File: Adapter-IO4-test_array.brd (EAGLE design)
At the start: 107.6 x 107.6 mm, 72 parts, among them Q1X11 p-fet, Q1X12 p-fet, Q1X21 p-fet, Q1X22 p-fet, Q2X11 p-fet, Q2X12 p-fet, Q2X21 p-fet, Q2X22 p-fet, Q3X11 p-fet, Q3X12 p-fet, Q3X21 p-fet, Q3X22 p-fet, Q4X11 p-fet, Q4X12 p-fet, Q4X21 p-fet, Q4X22 p-fet

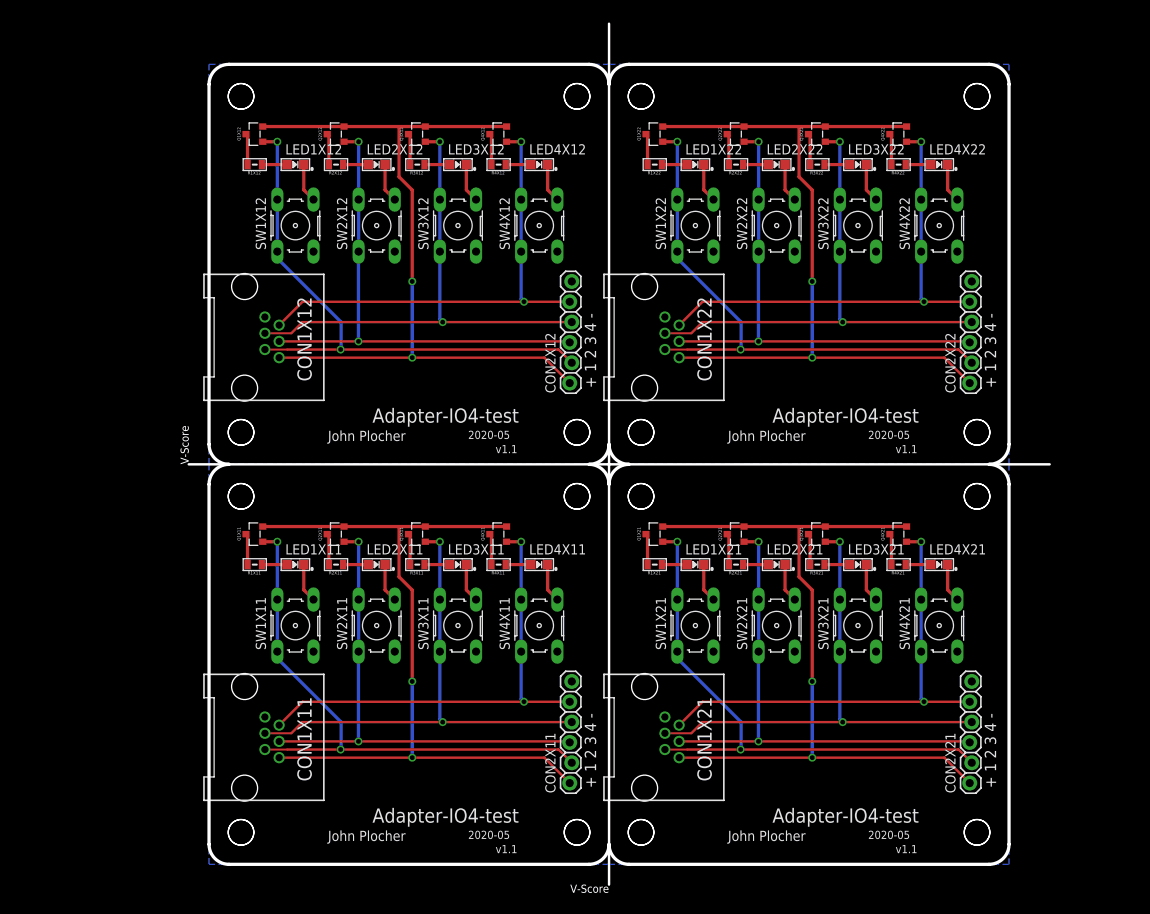
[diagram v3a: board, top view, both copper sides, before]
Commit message: fixed SPCoast lbr part orientation
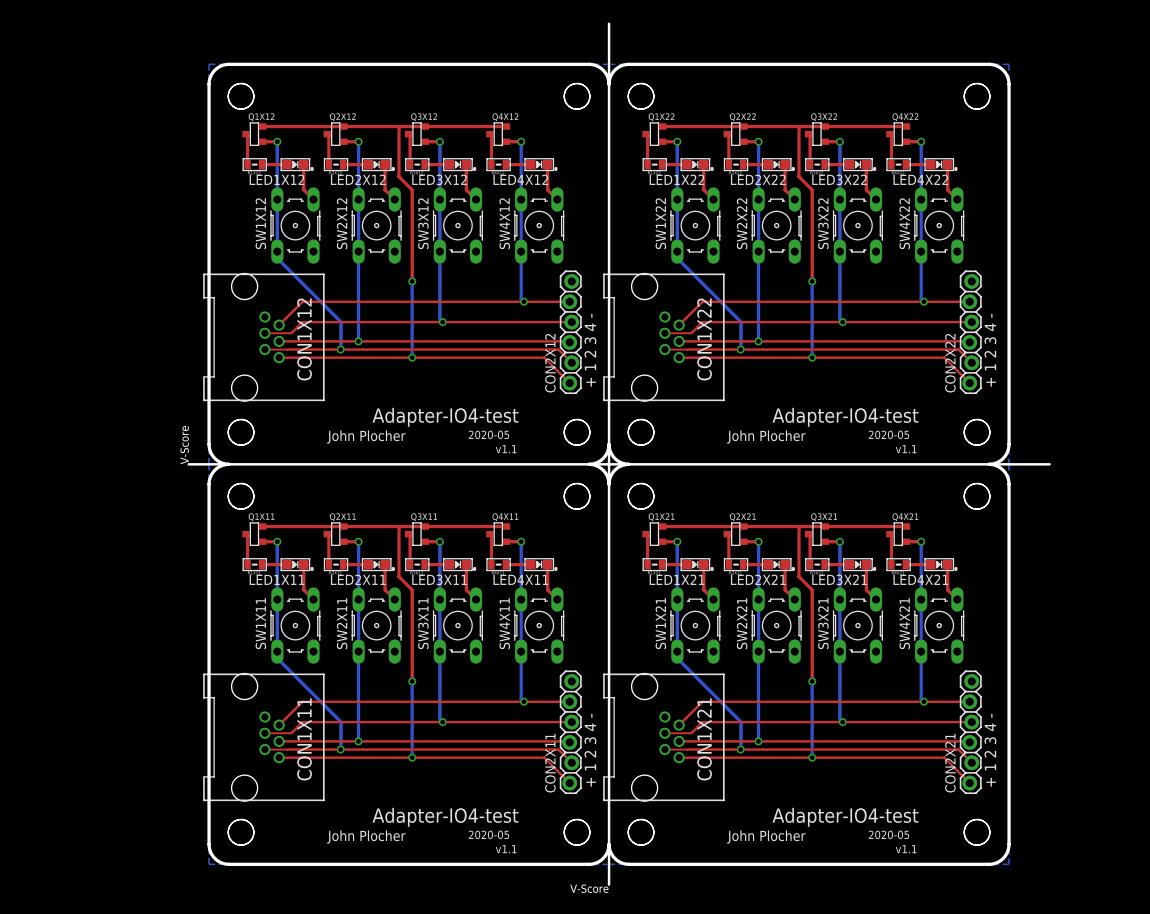
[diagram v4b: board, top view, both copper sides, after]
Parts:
- turned LED1X11 to 180 degrees
- turned LED1X12 to 180 degrees
- turned LED1X21 to 180 degrees
- turned LED1X22 to 180 degrees
- turned LED2X11 to 180 degrees
- turned LED2X12 to 180 degrees
- turned LED2X21 to 180 degrees
- turned LED2X22 to 180 degrees
- turned LED3X11 to 180 degrees
- turned LED3X12 to 180 degrees
- turned LED3X21 to 180 degrees
- turned LED3X22 to 180 degrees
- turned LED4X11 to 180 degrees
- turned LED4X12 to 180 degrees
- turned LED4X21 to 180 degrees
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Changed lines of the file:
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@@
 <element name="CON1X11" library="SPCoast" package="RJ25-INVERTED" value="" x="4.445" y="15.875" rot="R270"/>
 <element name="CON2X11" library="SPCoast" package="1X06_LOCK" value="" x="45.085" y="10.16" rot="R90"/>
-<element name="LED1X11" library="SPCoast" package="0805-LED" value="G" x="10.795" y="37.465"/>
-<element name="LED2X11" library="SPCoast" package="0805-LED" value="G" x="20.955" y="37.465"/>
-<element name="LED3X11" library="SPCoast" package="0805-LED" value="G" x="31.115" y="37.465"/>
-<element name="LED4X11" library="SPCoast" package="0805-LED" value="G" x="41.275" y="37.465"/>
-<element name="Q1X11" library="SPCoast" package="SOT23-3" value="p-fet" x="5.715" y="41.275" rot="R90"/>
-<element name="Q2X11" library="SPCoast" package="SOT23-3" value="p-fet" x="15.875" y="41.275" rot="R90"/>
-<element name="Q3X11" library="SPCoast" package="SOT23-3" value="p-fet" x="26.035" y="41.275" rot="R90"/>
-<element name="Q4X11" library="SPCoast" package="SOT23-3" value="p-fet" x="36.195" y="41.275" rot="R90"/>
+<element name="LED1X11" library="SPCoast" package="0805-LED" value="G" x="10.795" y="37.465" rot="R180"/>
+<element name="LED2X11" library="SPCoast" package="0805-LED" value="G" x="20.955" y="37.465" rot="R180"/>
+<element name="LED3X11" library="SPCoast" package="0805-LED" value="G" x="31.115" y="37.465" rot="R180"/>
+<element name="LED4X11" library="SPCoast" package="0805-LED" value="G" x="41.275" y="37.465" rot="R180"/>
+<element name="Q1X11" library="SPCoast" package="SOT23-3" value="p-fet" x="5.715" y="41.275"/>
+<element name="Q2X11" library="SPCoast" package="SOT23-3" value="p-fet" x="15.875" y="41.275"/>
+<element name="Q3X11" library="SPCoast" package="SOT23-3" value="p-fet" x="26.035" y="41.275"/>
+<element name="Q4X11" library="SPCoast" package="SOT23-3" value="p-fet" x="36.195" y="41.275"/>
 <element name="R1X11" library="SPCoast" package="0805-RES" value="2k0" x="5.715" y="37.465" rot="R180"/>
 <element name="R2X11" library="SPCoast" package="0805-RES" value="2k0" x="15.875" y="37.465" rot="R180"/>
@@
 <element name="CON1X12" library="SPCoast" package="RJ25-INVERTED" value="" x="4.445" y="65.875" rot="R270"/>
 <element name="CON2X12" library="SPCoast" package="1X06_LOCK" value="" x="45.085" y="60.16" rot="R90"/>
-<element name="LED1X12" library="SPCoast" package="0805-LED" value="G" x="10.795" y="87.465"/>
-<element name="LED2X12" library="SPCoast" package="0805-LED" value="G" x="20.955" y="87.465"/>
-<element name="LED3X12" library="SPCoast" package="0805-LED" value="G" x="31.115" y="87.465"/>
-<element name="LED4X12" library="SPCoast" package="0805-LED" value="G" x="41.275" y="87.465"/>
-<element name="Q1X12" library="SPCoast" package="SOT23-3" value="p-fet" x="5.715" y="91.275" rot="R90"/>
-<element name="Q2X12" library="SPCoast" package="SOT23-3" value="p-fet" x="15.875" y="91.275" rot="R90"/>
-<element name="Q3X12" library="SPCoast" package="SOT23-3" value="p-fet" x="26.035" y="91.275" rot="R90"/>
-<element name="Q4X12" library="SPCoast" package="SOT23-3" value="p-fet" x="36.195" y="91.275" rot="R90"/>
+<element name="LED1X12" library="SPCoast" package="0805-LED" value="G" x="10.795" y="87.465" rot="R180"/>
+<element name="LED2X12" library="SPCoast" package="0805-LED" value="G" x="20.955" y="87.465" rot="R180"/>
+<element name="LED3X12" library="SPCoast" package="0805-LED" value="G" x="31.115" y="87.465" rot="R180"/>
+<element name="LED4X12" library="SPCoast" package="0805-LED" value="G" x="41.275" y="87.465" rot="R180"/>
+<element name="Q1X12" library="SPCoast" package="SOT23-3" value="p-fet" x="5.715" y="91.275"/>
+<element name="Q2X12" library="SPCoast" package="SOT23-3" value="p-fet" x="15.875" y="91.275"/>
+<element name="Q3X12" library="SPCoast" package="SOT23-3" value="p-fet" x="26.035" y="91.275"/>
+<element name="Q4X12" library="SPCoast" package="SOT23-3" value="p-fet" x="36.195" y="91.275"/>
 <element name="R1X12" library="SPCoast" package="0805-RES" value="2k0" x="5.715" y="87.465" rot="R180"/>
 <element name="R2X12" library="SPCoast" package="0805-RES" value="2k0" x="15.875" y="87.465" rot="R180"/>
@@
 <element name="CON1X21" library="SPCoast" package="RJ25-INVERTED" value="" x="54.445" y="15.875" rot="R270"/>
 <element name="CON2X21" library="SPCoast" package="1X06_LOCK" value="" x="95.085" y="10.16" rot="R90"/>
-<element name="LED1X21" library="SPCoast" package="0805-LED" value="G" x="60.795" y="37.465"/>
-<element name="LED2X21" library="SPCoast" package="0805-LED" value="G" x="70.955" y="37.465"/>
-<element name="LED3X21" library="SPCoast" package="0805-LED" value="G" x="81.115" y="37.465"/>
-<element name="LED4X21" library="SPCoast" package="0805-LED" value="G" x="91.275" y="37.465"/>
-<element name="Q1X21" library="SPCoast" package="SOT23-3" value="p-fet" x="55.715" y="41.275" rot="R90"/>
-<element name="Q2X21" library="SPCoast" package="SOT23-3" value="p-fet" x="65.875" y="41.275" rot="R90"/>
-<element name="Q3X21" library="SPCoast" package="SOT23-3" value="p-fet" x="76.035" y="41.275" rot="R90"/>
-<element name="Q4X21" library="SPCoast" package="SOT23-3" value="p-fet" x="86.195" y="41.275" rot="R90"/>
+<element name="LED1X21" library="SPCoast" package="0805-LED" value="G" x="60.795" y="37.465" rot="R180"/>
+<element name="LED2X21" library="SPCoast" package="0805-LED" value="G" x="70.955" y="37.465" rot="R180"/>
+<element name="LED3X21" library="SPCoast" package="0805-LED" value="G" x="81.115" y="37.465" rot="R180"/>
+<element name="LED4X21" library="SPCoast" package="0805-LED" value="G" x="91.275" y="37.465" rot="R180"/>
+<element name="Q1X21" library="SPCoast" package="SOT23-3" value="p-fet" x="55.715" y="41.275"/>
+<element name="Q2X21" library="SPCoast" package="SOT23-3" value="p-fet" x="65.875" y="41.275"/>
+<element name="Q3X21" library="SPCoast" package="SOT23-3" value="p-fet" x="76.035" y="41.275"/>
+<element name="Q4X21" library="SPCoast" package="SOT23-3" value="p-fet" x="86.195" y="41.275"/>
 <element name="R1X21" library="SPCoast" package="0805-RES" value="2k0" x="55.715" y="37.465" rot="R180"/>
 <element name="R2X21" library="SPCoast" package="0805-RES" value="2k0" x="65.875" y="37.465" rot="R180"/>
@@
 <element name="CON1X22" library="SPCoast" package="RJ25-INVERTED" value="" x="54.445" y="65.875" rot="R270"/>
 <element name="CON2X22" library="SPCoast" package="1X06_LOCK" value="" x="95.085" y="60.16" rot="R90"/>
-<element name="LED1X22" library="SPCoast" package="0805-LED" value="G" x="60.795" y="87.465"/>
-<element name="LED2X22" library="SPCoast" package="0805-LED" value="G" x="70.955" y="87.465"/>
-<element name="LED3X22" library="SPCoast" package="0805-LED" value="G" x="81.115" y="87.465"/>
-<element name="LED4X22" library="SPCoast" package="0805-LED" value="G" x="91.275" y="87.465"/>
-<element name="Q1X22" library="SPCoast" package="SOT23-3" value="p-fet" x="55.715" y="91.275" rot="R90"/>
-<element name="Q2X22" library="SPCoast" package="SOT23-3" value="p-fet" x="65.875" y="91.275" rot="R90"/>
-<element name="Q3X22" library="SPCoast" package="SOT23-3" value="p-fet" x="76.035" y="91.275" rot="R90"/>
-<element name="Q4X22" library="SPCoast" package="SOT23-3" value="p-fet" x="86.195" y="91.275" rot="R90"/>
+<element name="LED1X22" library="SPCoast" package="0805-LED" value="G" x="60.795" y="87.465" rot="R180"/>
+<element name="LED2X22" library="SPCoast" package="0805-LED" value="G" x="70.955" y="87.465" rot="R180"/>
+<element name="LED3X22" library="SPCoast" package="0805-LED" value="G" x="81.115" y="87.465" rot="R180"/>
+<element name="LED4X22" library="SPCoast" package="0805-LED" value="G" x="91.275" y="87.465" rot="R180"/>
+<element name="Q1X22" library="SPCoast" package="SOT23-3" value="p-fet" x="55.715" y="91.275"/>
+<element name="Q2X22" library="SPCoast" package="SOT23-3" value="p-fet" x="65.875" y="91.275"/>
+<element name="Q3X22" library="SPCoast" package="SOT23-3" value="p-fet" x="76.035" y="91.275"/>
+<element name="Q4X22" library="SPCoast" package="SOT23-3" value="p-fet" x="86.195" y="91.275"/>
 <element name="R1X22" library="SPCoast" package="0805-RES" value="2k0" x="55.715" y="87.465" rot="R180"/>
 <element name="R2X22" library="SPCoast" package="0805-RES" value="2k0" x="65.875" y="87.465" rot="R180"/>

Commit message: added values for connectors
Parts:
- CON1X11, CON1X12, CON1X21, CON1X22: value (none) -> RJ12/6
- CON2X11, CON2X12, CON2X21, CON2X22: value (none) -> 0.100
- SW1X11, SW1X12, SW1X21, SW1X22, SW2X11, SW2X12, SW2X21, SW2X22, SW3X11, SW3X12, SW3X21, SW3X22, SW4X11, SW4X12, SW4X21, SW4X22: value (none) -> SPST-MOM
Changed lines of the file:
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@@
 </autorouter>
 <elements>
-<element name="CON1X11" library="SPCoast" package="RJ25-INVERTED" value="" x="4.445" y="15.875" rot="R270"/>
-<element name="CON2X11" library="SPCoast" package="1X06_LOCK" value="" x="45.085" y="10.16" rot="R90"/>
+<element name="CON1X11" library="SPCoast" package="RJ25-INVERTED" value="RJ12/6" x="4.445" y="15.875" rot="R270"/>
+<element name="CON2X11" library="SPCoast" package="1X06_LOCK" value="0.100" x="45.085" y="10.16" rot="R90"/>
 <element name="LED1X11" library="SPCoast" package="0805-LED" value="G" x="10.795" y="37.465" rot="R180"/>
 <element name="LED2X11" library="SPCoast" package="0805-LED" value="G" x="20.955" y="37.465" rot="R180"/>
@@
 <element name="R3X11" library="SPCoast" package="0805-RES" value="2k0" x="26.035" y="37.465" rot="R180"/>
 <element name="R4X11" library="SPCoast" package="0805-RES" value="2k0" x="36.195" y="37.465" rot="R180"/>
-<element name="SW1X11" library="SPCoast" package="B3F-10XX" value="" x="10.795" y="29.845" rot="R90"/>
-<element name="SW2X11" library="SPCoast" package="B3F-10XX" value="" x="20.955" y="29.845" rot="R90"/>
-<element name="SW3X11" library="SPCoast" package="B3F-10XX" value="" x="31.115" y="29.845" rot="R90"/>
-<element name="SW4X11" library="SPCoast" package="B3F-10XX" value="" x="41.275" y="29.845" rot="R90"/>
-<element name="CON1X12" library="SPCoast" package="RJ25-INVERTED" value="" x="4.445" y="65.875" rot="R270"/>
-<element name="CON2X12" library="SPCoast" package="1X06_LOCK" value="" x="45.085" y="60.16" rot="R90"/>
+<element name="SW1X11" library="SPCoast" package="B3F-10XX" value="SPST-MOM" x="10.795" y="29.845" rot="R90"/>
+<element name="SW2X11" library="SPCoast" package="B3F-10XX" value="SPST-MOM" x="20.955" y="29.845" rot="R90"/>
+<element name="SW3X11" library="SPCoast" package="B3F-10XX" value="SPST-MOM" x="31.115" y="29.845" rot="R90"/>
+<element name="SW4X11" library="SPCoast" package="B3F-10XX" value="SPST-MOM" x="41.275" y="29.845" rot="R90"/>
+<element name="CON1X12" library="SPCoast" package="RJ25-INVERTED" value="RJ12/6" x="4.445" y="65.875" rot="R270"/>
+<element name="CON2X12" library="SPCoast" package="1X06_LOCK" value="0.100" x="45.085" y="60.16" rot="R90"/>
 <element name="LED1X12" library="SPCoast" package="0805-LED" value="G" x="10.795" y="87.465" rot="R180"/>
 <element name="LED2X12" library="SPCoast" package="0805-LED" value="G" x="20.955" y="87.465" rot="R180"/>
@@
 <element name="R3X12" library="SPCoast" package="0805-RES" value="2k0" x="26.035" y="87.465" rot="R180"/>
 <element name="R4X12" library="SPCoast" package="0805-RES" value="2k0" x="36.195" y="87.465" rot="R180"/>
-<element name="SW1X12" library="SPCoast" package="B3F-10XX" value="" x="10.795" y="79.845" rot="R90"/>
-<element name="SW2X12" library="SPCoast" package="B3F-10XX" value="" x="20.955" y="79.845" rot="R90"/>
-<element name="SW3X12" library="SPCoast" package="B3F-10XX" value="" x="31.115" y="79.845" rot="R90"/>
-<element name="SW4X12" library="SPCoast" package="B3F-10XX" value="" x="41.275" y="79.845" rot="R90"/>
-<element name="CON1X21" library="SPCoast" package="RJ25-INVERTED" value="" x="54.445" y="15.875" rot="R270"/>
-<element name="CON2X21" library="SPCoast" package="1X06_LOCK" value="" x="95.085" y="10.16" rot="R90"/>
+<element name="SW1X12" library="SPCoast" package="B3F-10XX" value="SPST-MOM" x="10.795" y="79.845" rot="R90"/>
+<element name="SW2X12" library="SPCoast" package="B3F-10XX" value="SPST-MOM" x="20.955" y="79.845" rot="R90"/>
+<element name="SW3X12" library="SPCoast" package="B3F-10XX" value="SPST-MOM" x="31.115" y="79.845" rot="R90"/>
+<element name="SW4X12" library="SPCoast" package="B3F-10XX" value="SPST-MOM" x="41.275" y="79.845" rot="R90"/>
+<element name="CON1X21" library="SPCoast" package="RJ25-INVERTED" value="RJ12/6" x="54.445" y="15.875" rot="R270"/>
+<element name="CON2X21" library="SPCoast" package="1X06_LOCK" value="0.100" x="95.085" y="10.16" rot="R90"/>
 <element name="LED1X21" library="SPCoast" package="0805-LED" value="G" x="60.795" y="37.465" rot="R180"/>
 <element name="LED2X21" library="SPCoast" package="0805-LED" value="G" x="70.955" y="37.465" rot="R180"/>
@@
 <element name="R3X21" library="SPCoast" package="0805-RES" value="2k0" x="76.035" y="37.465" rot="R180"/>
 <element name="R4X21" library="SPCoast" package="0805-RES" value="2k0" x="86.195" y="37.465" rot="R180"/>
-<element name="SW1X21" library="SPCoast" package="B3F-10XX" value="" x="60.795" y="29.845" rot="R90"/>
-<element name="SW2X21" library="SPCoast" package="B3F-10XX" value="" x="70.955" y="29.845" rot="R90"/>
-<element name="SW3X21" library="SPCoast" package="B3F-10XX" value="" x="81.115" y="29.845" rot="R90"/>
-<element name="SW4X21" library="SPCoast" package="B3F-10XX" value="" x="91.275" y="29.845" rot="R90"/>
-<element name="CON1X22" library="SPCoast" package="RJ25-INVERTED" value="" x="54.445" y="65.875" rot="R270"/>
-<element name="CON2X22" library="SPCoast" package="1X06_LOCK" value="" x="95.085" y="60.16" rot="R90"/>
+<element name="SW1X21" library="SPCoast" package="B3F-10XX" value="SPST-MOM" x="60.795" y="29.845" rot="R90"/>
+<element name="SW2X21" library="SPCoast" package="B3F-10XX" value="SPST-MOM" x="70.955" y="29.845" rot="R90"/>
+<element name="SW3X21" library="SPCoast" package="B3F-10XX" value="SPST-MOM" x="81.115" y="29.845" rot="R90"/>
+<element name="SW4X21" library="SPCoast" package="B3F-10XX" value="SPST-MOM" x="91.275" y="29.845" rot="R90"/>
+<element name="CON1X22" library="SPCoast" package="RJ25-INVERTED" value="RJ12/6" x="54.445" y="65.875" rot="R270"/>
+<element name="CON2X22" library="SPCoast" package="1X06_LOCK" value="0.100" x="95.085" y="60.16" rot="R90"/>
 <element name="LED1X22" library="SPCoast" package="0805-LED" value="G" x="60.795" y="87.465" rot="R180"/>
 <element name="LED2X22" library="SPCoast" package="0805-LED" value="G" x="70.955" y="87.465" rot="R180"/>
@@
 <element name="R3X22" library="SPCoast" package="0805-RES" value="2k0" x="76.035" y="87.465" rot="R180"/>
 <element name="R4X22" library="SPCoast" package="0805-RES" value="2k0" x="86.195" y="87.465" rot="R180"/>
-<element name="SW1X22" library="SPCoast" package="B3F-10XX" value="" x="60.795" y="79.845" rot="R90"/>
-<element name="SW2X22" library="SPCoast" package="B3F-10XX" value="" x="70.955" y="79.845" rot="R90"/>
-<element name="SW3X22" library="SPCoast" package="B3F-10XX" value="" x="81.115" y="79.845" rot="R90"/>
-<element name="SW4X22" library="SPCoast" package="B3F-10XX" value="" x="91.275" y="79.845" rot="R90"/>
+<element name="SW1X22" library="SPCoast" package="B3F-10XX" value="SPST-MOM" x="60.795" y="79.845" rot="R90"/>
+<element name="SW2X22" library="SPCoast" package="B3F-10XX" value="SPST-MOM" x="70.955" y="79.845" rot="R90"/>
+<element name="SW3X22" library="SPCoast" package="B3F-10XX" value="SPST-MOM" x="81.115" y="79.845" rot="R90"/>
+<element name="SW4X22" library="SPCoast" package="B3F-10XX" value="SPST-MOM" x="91.275" y="79.845" rot="R90"/>
 </elements>
 <signals>
